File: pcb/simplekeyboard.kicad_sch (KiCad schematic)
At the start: 23 parts, among them J1 USB_C_Receptacle_USB2.0_16P, SW62 SW_SPDT, SW63 SW_Push, U1 STM32F072CBT6, U2 USBLC6-2SC6, U3 LD39050PU33R

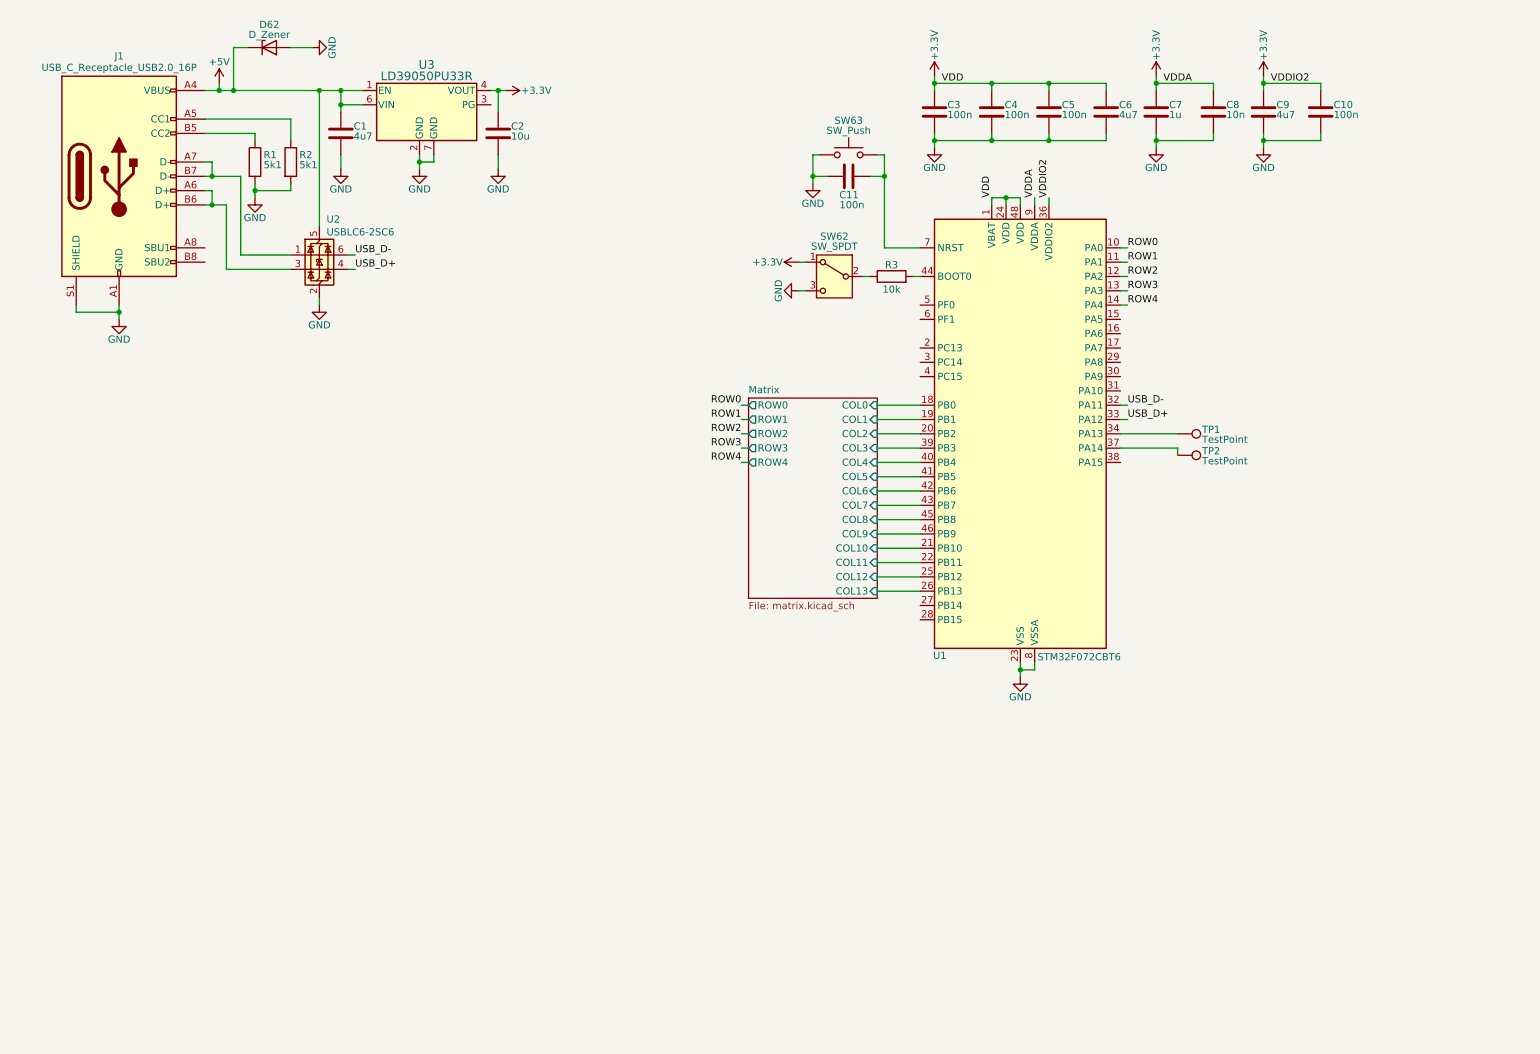
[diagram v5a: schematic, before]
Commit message: IO expanders in schematic
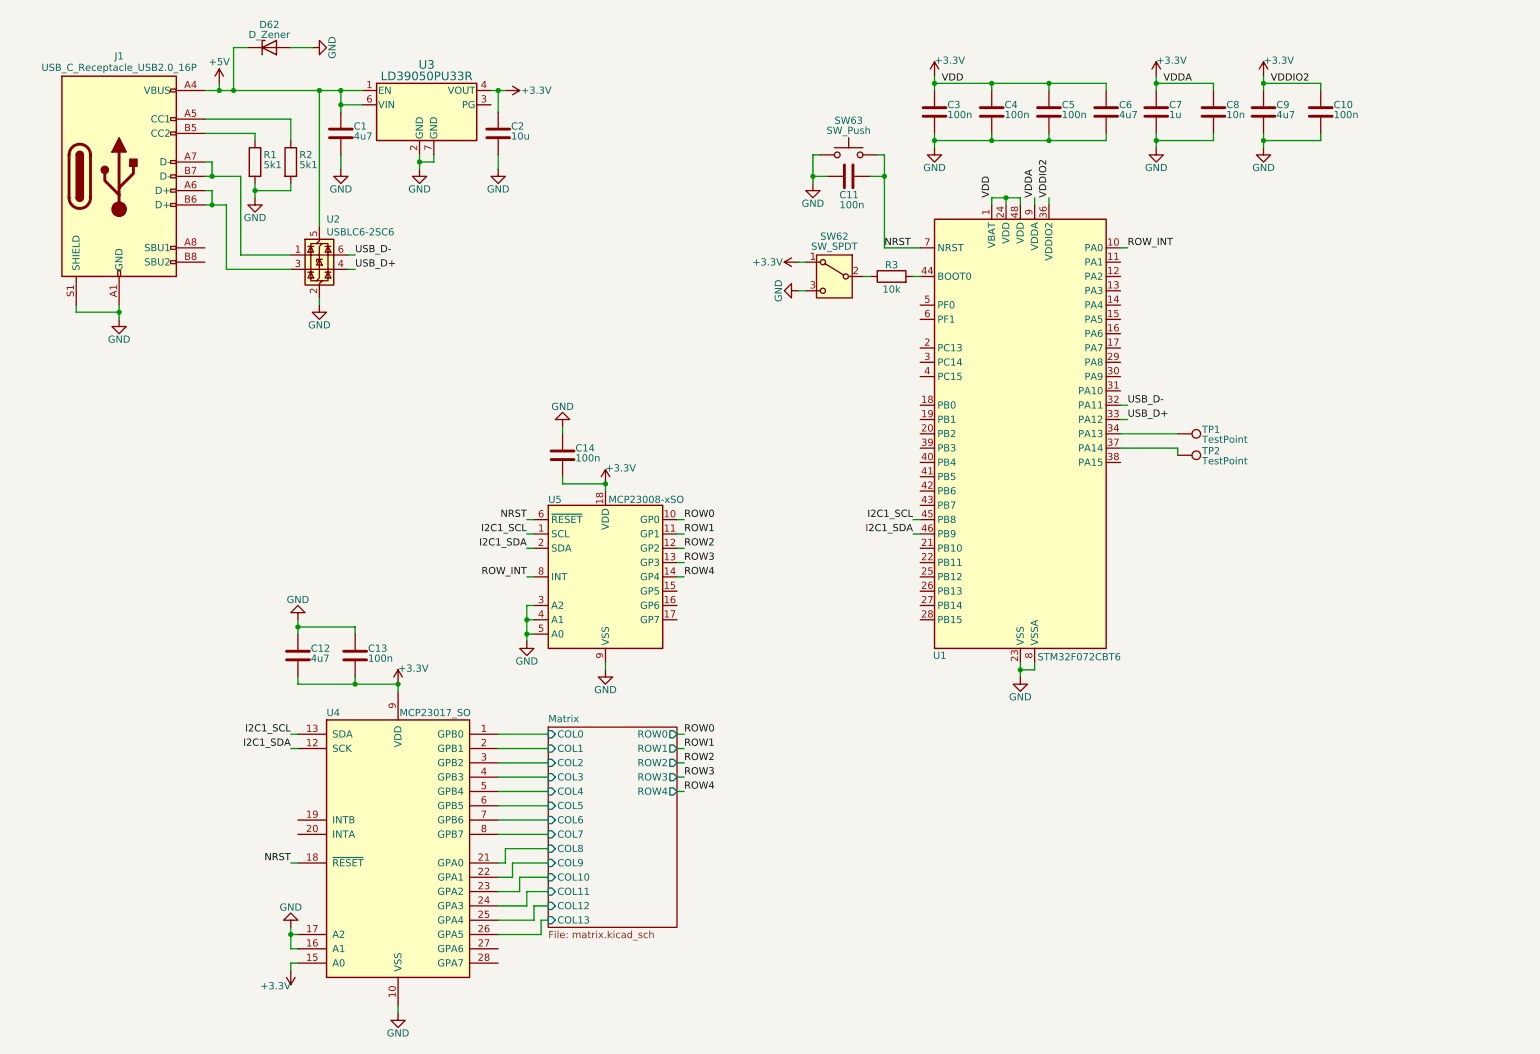
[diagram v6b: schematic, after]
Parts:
- added C12: 4u7, Capacitor_SMD:C_0603_1608Metric, symbol Device:C
- added C13, C14: 100n, Capacitor_SMD:C_0603_1608Metric, symbol Device:C
- added U4: MCP23017_SO, Package_SO:SOIC-28W_7.5x17.9mm_P1.27mm, symbol Interface_Expansion:MCP23017_SO
- added U5: MCP23008-xSO, Package_SO:SOIC-18W_7.5x11.6mm_P1.27mm, symbol Interface_Expansion:MCP23008-xSO
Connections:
- net +3.3V: now also C12.2, C13.2, C14.2, U4.15 (A0), U4.9 (VDD), U5.18 (VDD)
- net GND: now also C12.1, C13.1, C14.1, U4.10 (VSS), U4.16 (A1), U4.17 (A2), U5.3 (A2), U5.4 (A1), U5.5 (A0), U5.9 (VSS)
- net Matrix/COL0: now also U4.1 (GPB0); no longer U1.18 (PB0)
- net Matrix/COL1: now also U4.2 (GPB1); no longer U1.19 (PB1)
- net Matrix/COL10: now also U4.23 (GPA2); no longer U1.21 (PB10)
- net Matrix/COL11: now also U4.24 (GPA3); no longer U1.22 (PB11)
- net Matrix/COL12: now also U4.25 (GPA4); no longer U1.25 (PB12)
- net Matrix/COL13: now also U4.26 (GPA5); no longer U1.26 (PB13)
- net Matrix/COL2: now also U4.3 (GPB2); no longer U1.20 (PB2)
- net Matrix/COL3: now also U4.4 (GPB3); no longer U1.39 (PB3)
- net Matrix/COL4: now also U4.5 (GPB4); no longer U1.40 (PB4)
- net Matrix/COL5: now also U4.6 (GPB5); no longer U1.41 (PB5)
- net Matrix/COL6: now also U4.7 (GPB6); no longer U1.42 (PB6)
- net Matrix/COL7: now also U4.8 (GPB7); no longer U1.43 (PB7)
- net Matrix/COL8: now also U4.21 (GPA0); no longer U1.45 (PB8)
- net Matrix/COL9: now also U4.22 (GPA1); no longer U1.46 (PB9)
- net ROW0: now also U5.10 (GP0); no longer U1.10 (PA0)
- net ROW1: now also U5.11 (GP1); no longer U1.11 (PA1)
- net ROW2: now also U5.12 (GP2); no longer U1.12 (PA2)
- net ROW3: now also U5.13 (GP3); no longer U1.13 (PA3)
- net ROW4: now also U5.14 (GP4); no longer U1.14 (PA4)
- net NRST: now reaches C11.2, SW63.2, U1.7 (NRST)
- net NRST: now also U4.18 (~{RESET}), U5.6 (~{RESET})
- new net I2C1_SCL: U1.45 (PB8), U4.13 (SDA), U5.1 (SCL)
- new net I2C1_SDA: U1.46 (PB9), U4.12 (SCK), U5.2 (SDA)
- new net ROW_INT: U1.10 (PA0), U5.8 (INT)

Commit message: Fix I2C bus
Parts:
- added R4, R5: 2k2, Resistor_SMD:R_0603_1608Metric, symbol Device:R
- added R6, R7: 10k, Resistor_SMD:R_0603_1608Metric, symbol Device:R
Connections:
- net +3.3V: now also R4.1, R5.1, R6.1, R7.1
- net I2C1_SCL: now also R4.2
- net I2C1_SDA: now also R5.2
- net NRST: now also R7.2
- net ROW_INT: now also R6.2
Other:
- moved on the sheet: C10, C3, C4, C5, C6, C7, C8, C9

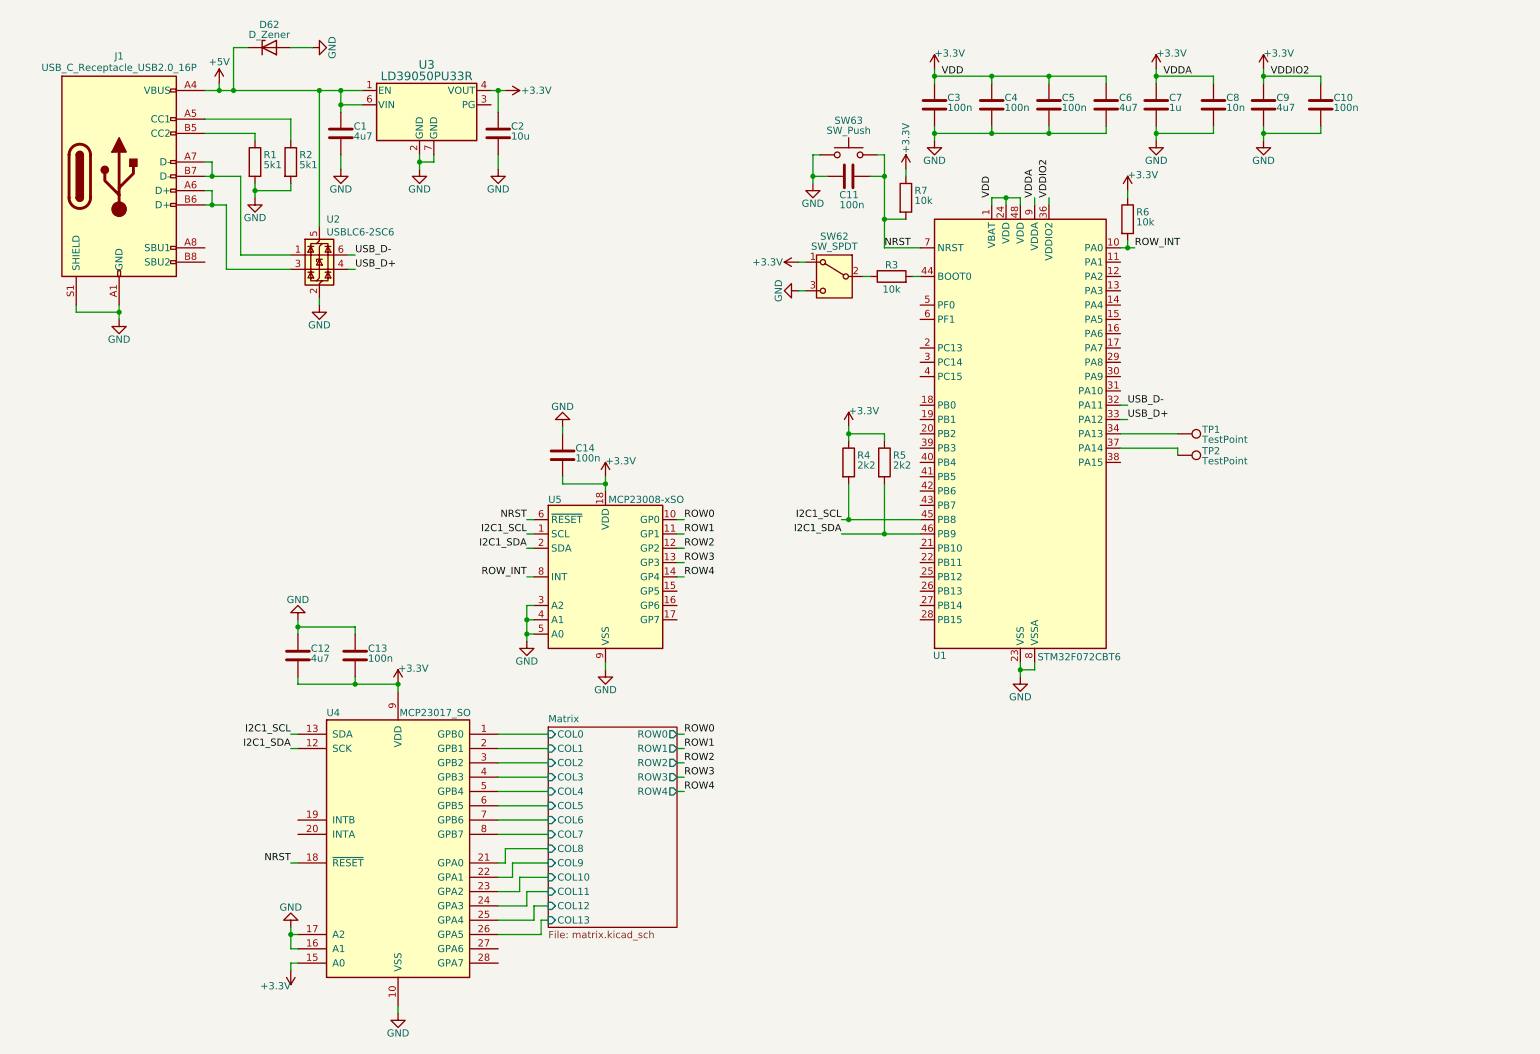
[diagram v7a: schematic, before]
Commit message: Finish and validate schematic
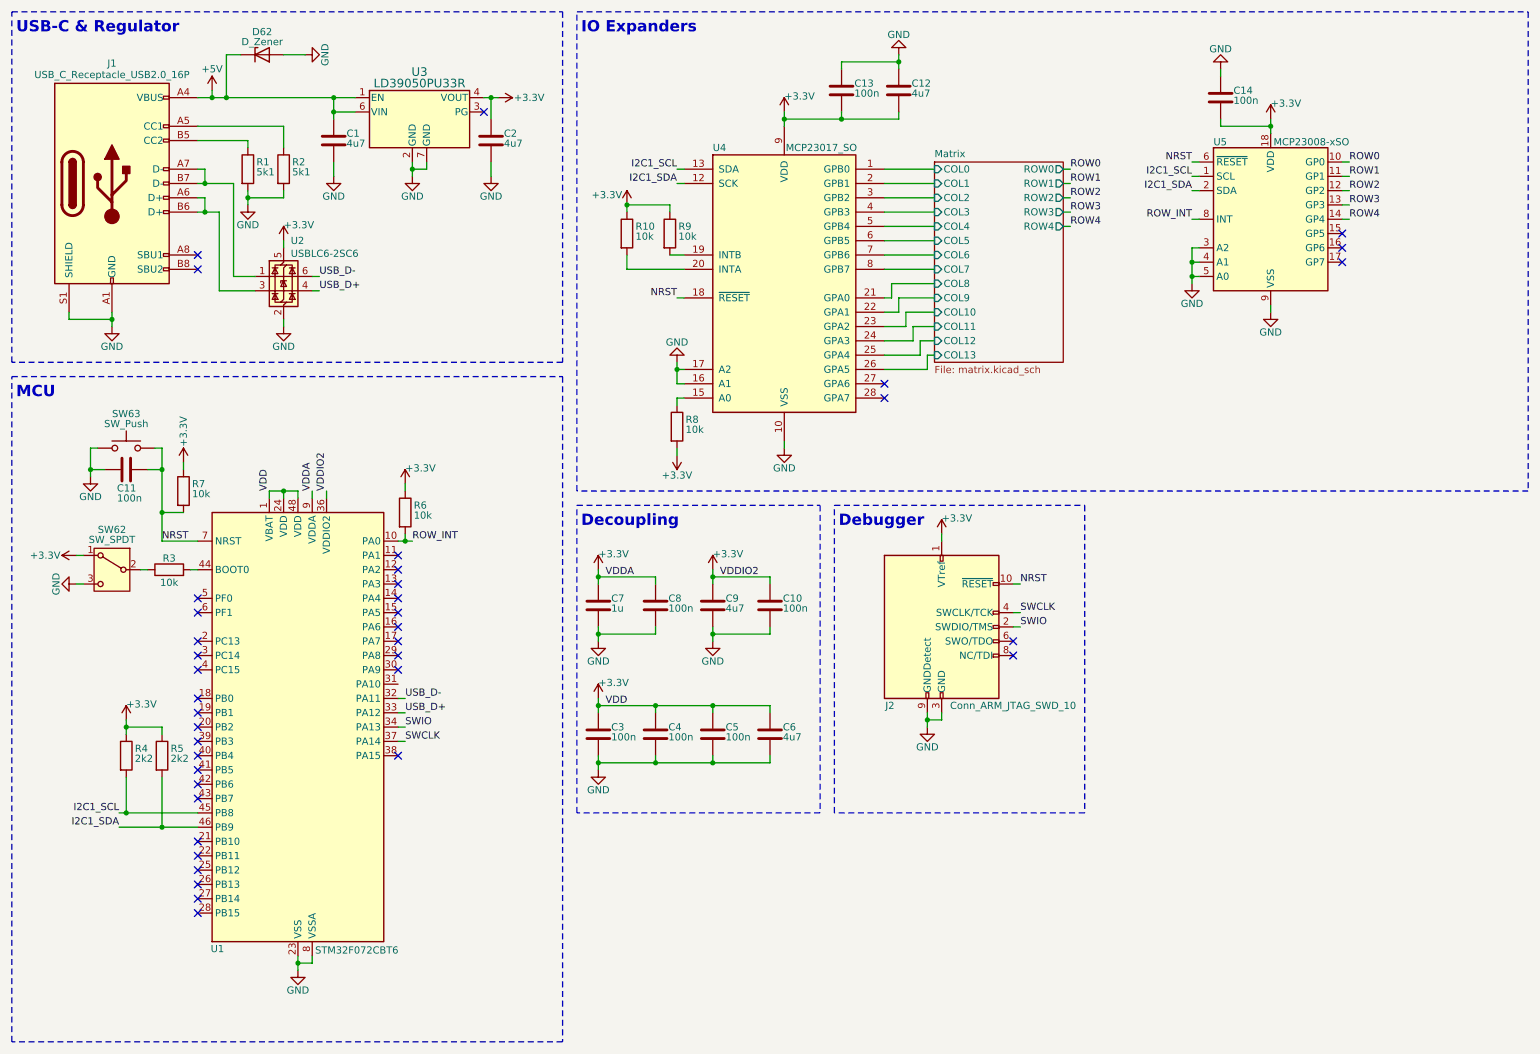
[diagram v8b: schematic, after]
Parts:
- removed TP1, TP2: TestPoint, TestPoint:TestPoint_Pad_1.0x1.0mm, symbol Connector:TestPoint
- added J2: Conn_ARM_JTAG_SWD_10, Connector_PinHeader_1.27mm:PinHeader_2x05_P1.27mm_Horizontal, symbol Connector:Conn_ARM_JTAG_SWD_10
- added R10, R8, R9: 10k, Resistor_SMD:R_0603_1608Metric, symbol Device:R
- C2: value 10u -> 4u7
- C8: value 10n -> 100n
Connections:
- net +3.3V: now also U2.5 (VBUS), J2.1 (VTref), R10.1, R8.2, R9.1; no longer U4.15 (A0)
- net +5V: no longer U2.5 (VBUS)
- net GND: now also J2.3 (GND), J2.5 (GND), J2.9 (GNDDetect)
- net NRST: now also J2.10 (~{RESET})
- net SWIO: now reaches U1.34 (PA13)
- net SWIO: now also J2.2 (SWDIO/TMS)
- net SWCLK: now reaches U1.37 (PA14)
- net SWCLK: now also J2.4 (SWCLK/TCK)
- net at U4.19 (INTB): now also R9.2
- net at U4.20 (INTA): now also R10.2
- new net: R8.1, U4.15 (A0)
- no-connect marks 0 -> 39
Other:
- note added: "Debugger"
- note added: "Decoupling"
- note added: "IO Expanders"
- note added: "MCU"
- note added: "USB-C & Regulator"
- title: (none) -> simplekeyboard
- moved on the sheet: C1, C10, C11, C12, C13, C14, C2, C3, C4, C5, C6, C7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
